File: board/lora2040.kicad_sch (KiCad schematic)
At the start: 22 parts, among them U1 RP2040, U2 MR20H40, U3 RFM9xBreakout, Y1 ABM8-272-T3

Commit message: added in sx1262 ref design
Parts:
- removed U3: RFM9xBreakout, RF_Module:HOPERF_RFM9XW_SMD, symbol symbols:RFM9xBreakout
- added C1: 47nF, custom-footprints:sx126x_C_0201, symbol Device:C_Small
- added C14, C15: 1nF, custom-footprints:sx126x_C_0201, symbol Device:C_Small
- added C16: 0.1uF, Capacitor_SMD:C_0402_1005Metric, symbol Device:C_Small
- added C17: 470nF, Capacitor_SMD:C_0402_1005Metric, symbol Device:C_Small
- added C18: 0.1uF, custom-footprints:sx126x_C_0201, symbol Device:C_Small
- added C2: 47pF, custom-footprints:sx126x_C_0201, symbol Device:C_Small
- added C21: 0.1uF, custom-footprints:sx126x_C_0201, symbol Device:C
- added C8: 39pF, custom-footprints:sx126x_C_0201, symbol Device:C_Small
- added J1: u.FL, Connector_Coaxial:U.FL_Hirose_U.FL-R-SMT-1_Vertical, symbol Connector:Conn_Coaxial
- added L1: 47nF, custom-footprints:sx126x_L_0402, symbol Device:L
- added L7: 15uH, custom-footprints:sx126x_L_0805, symbol Device:L
- added R3, R4: 100, custom-footprints:sx126x_R_0201, symbol Device:R_US
- added R9: 10K, custom-footprints:sx126x_R_0201, symbol Device:R_US
- added U1: SX1262IMLTRT, custom-footprints:VQFN24_4X4MM_SX126x, symbol RF:SX1262IMLTRT
- added U2: BGS12WN6E6327, Package_LGA:Infineon_PG-TSNP-6-10_0.7x1.1mm_0.7x1.1mm_P0.4mm, symbol RF_Switch:BGS12WN6E6327
- added U3: 0900FM15K0039, custom-footprints:0900FM15K0039, symbol Filter:0900FM15K0039
- added Y1: EXS00A-CS06465, custom-footprints:sx126x_Xtal, symbol Device:Crystal_GND24
- C10: renamed from C7; footprint Capacitor_SMD:C_0402_1005Metric -> custom-footprints:sx126x_C_0201
- C11: renamed from C8; footprint Capacitor_SMD:C_0402_1005Metric -> custom-footprints:sx126x_C_0201
- C12: renamed from C9; footprint Capacitor_SMD:C_0402_1005Metric -> custom-footprints:sx126x_C_0201
- C13: renamed from C10; footprint Capacitor_SMD:C_0402_1005Metric -> custom-footprints:sx126x_C_0201
- C3: renamed from C1; footprint Capacitor_SMD:C_0402_1005Metric -> custom-footprints:sx126x_C_0201
- C4: renamed from C2; footprint Capacitor_SMD:C_0402_1005Metric -> custom-footprints:sx126x_C_0201
- C5: footprint Capacitor_SMD:C_0402_1005Metric -> custom-footprints:sx126x_C_0201
- C6: renamed from C4; footprint Capacitor_SMD:C_0402_1005Metric -> custom-footprints:sx126x_C_0201
- R1: renamed from R4; footprint Resistor_SMD:R_0402_1005Metric -> custom-footprints:sx126x_R_0201
- R2: renamed from R5; footprint Resistor_SMD:R_0402_1005Metric -> custom-footprints:sx126x_R_0201
- R5: renamed from R6; footprint Resistor_SMD:R_0402_1005Metric -> custom-footprints:sx126x_R_0201
- R6: renamed from R1; footprint Resistor_SMD:R_0402_1005Metric -> custom-footprints:sx126x_R_0201
- R7: renamed from R3; footprint Resistor_SMD:R_0402_1005Metric -> custom-footprints:sx126x_R_0201
- R8: renamed from R2; footprint Resistor_SMD:R_0402_1005Metric -> custom-footprints:sx126x_R_0201
- U4: renamed from U2; value MR20H40 -> MR20H40 or AS3004204
- renumbered C11 to C19, C12 to C20, C3 to C7, C6 to C9, U1 to U5, Y1 to Y2
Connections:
- net +3V3: now also C21.2, R9.2
- net GND: now also C10.1, C11.1, C12.1, C13.1, C19.1, C20.1, Y2.2, Y2.4, C1.1, C14.1, C15.1, C16.2, C17.1, C18.2, C2.1, C21.1, J1.2 (Ext), U1.2 (GND), U1.20 (GND), U1.25 (GND), U1.5 (GND), U1.8 (GND), U2.2 (GND), U3.10 (GND), U3.2 (GND), U3.5 (GND), U3.7 (GND), U3.9 (GND), Y1.2, Y1.4; no longer Y2.1, Y2.3
- net XIN: now also Y2.1; no longer Y2.2
- net at U5.26 (RUN): now also R9.1
- net SPI0_MISO_RX: now reaches U5.27 (GPIO16)
- net SPI0_MISO_RX: now also U1.16 (MISO)
- net SPI0_CS: now reaches U5.28 (GPIO17)
- net SPI0_CS: now also U1.19 (NSS)
- net SPI0_SCK: now reaches U5.29 (GPIO18)
- net SPI0_SCK: now also U1.18 (SCK)
- net SPI0_MOSI_TX: now reaches U5.30 (GPIO19)
- net SPI0_MOSI_TX: now also U1.17 (MOSI)
- net RF_RST: now reaches U5.31 (GPIO20)
- net RF_RST: now also U1.15 (~{RESET})
- net RF_BUSY: now reaches U5.32 (GPIO21)
- net RF_BUSY: now also U1.14 (BUSY)
- net RF_DIO1: now reaches U5.37 (GPIO25)
- net RF_DIO1: now also U1.13 (DIO1)
- net at C4.2, R8.1: now also Y2.3; no longer Y2.4
- new net: L1.2, U1.23 (RFO), U3.1 (RFO)
- new net: U1.22 (RFI_N), U3.3 (RFI_N)
- new net: U1.21 (RFI_P), U3.4 (RFI_P)
- new net: U2.3 (RF1), U3.6 (SW_RFI)
- new net: U2.1 (RF2), U3.8 (SW_RFO)
- new net: C1.2, C2.2, L1.1, U1.24 (VR_PA)
- new net: C15.2, R3.1, U2.4 (VDD)
- new net: C17.2, L7.2, U1.7 (VREG)
- new net: C8.1, J1.1 (In)
- new net: L7.1, U1.9 (DCC_SW)
- new net: U1.3 (XTA), Y1.3
- new net: U1.4 (XTB), Y1.1
- new net: C8.2, U2.5 (RFIN)
- new net: C14.2, R4.2, U2.6 (CTRL)
- new net ANT_SW: R3.2
- new net RF_DIO2: R4.1, U1.12 (DIO2)
- new net RF_DIO3: U1.6 (DIO3)
- new net VDD_RF: C16.1, C18.1, U1.1 (VDD_IN), U1.10 (VBAT), U1.11 (VBAT_IO)
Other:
- note added: "Based on Semtech PCB_E588V01A v1a"
- note added: "short for bootloader"
- note removed: "Switch to SX126x?"
- moved on the sheet: C10, C11, C12, C13, C19, C20, C3, C4, C5, C6, C7, C9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

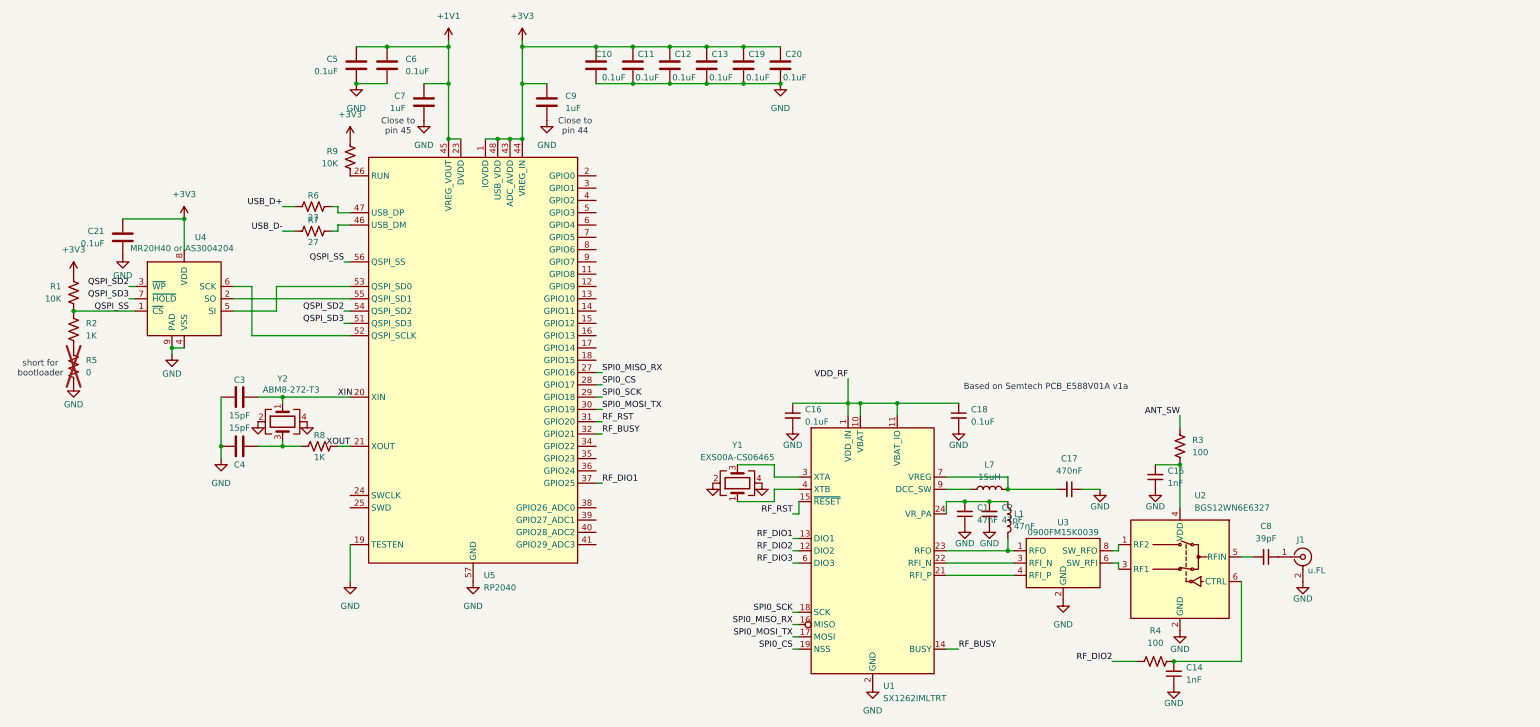
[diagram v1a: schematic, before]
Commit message: about to switch to TXCO
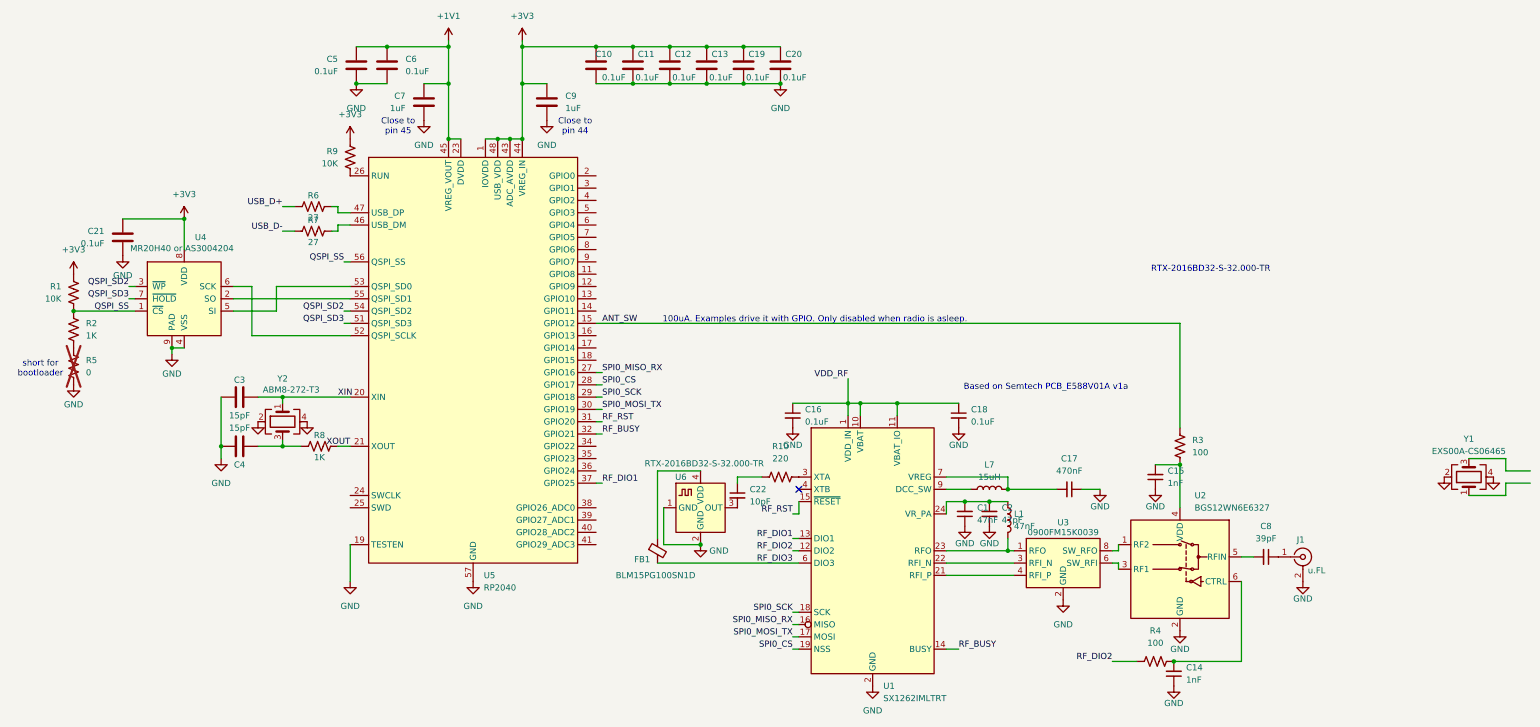
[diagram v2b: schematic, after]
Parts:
- added C22: 10pF, Capacitor_SMD:C_0402_1005Metric, symbol Device:C_Small
- added FB1: BLM15PG100SN1D, symbol Device:FerriteBead_Small
- added R10: 220, custom-footprints:sx126x_R_0201, symbol Device:R_US
- added U6: RTX-2016BD32-S-32.000-TR, custom-footprints:TXCO_2.0x1.6, symbol symbols:RTX-2016BD32-S-32.000-TR
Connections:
- net ANT_SW: now also U5.15 (GPIO12)
- net GND: now also U6.1 (GND), U6.2 (GND)
- net RF_DIO3: now also FB1.2
- net at U1.3 (XTA): now also R10.2; no longer Y1.3
- net at U1.4 (XTB): no longer Y1.1
- new net: FB1.1, U6.4 (VDD)
- new net: C22.2, U6.3 (OUT)
- new net: C22.1, R10.1
- no-connect marks 0 -> 1
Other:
- note added: "100uA. Examples drive it with GPIO. Only disabled when radio is asleep."
- note added: "RTX-2016BD32-S-32.000-TR"
- moved on the sheet: Y1

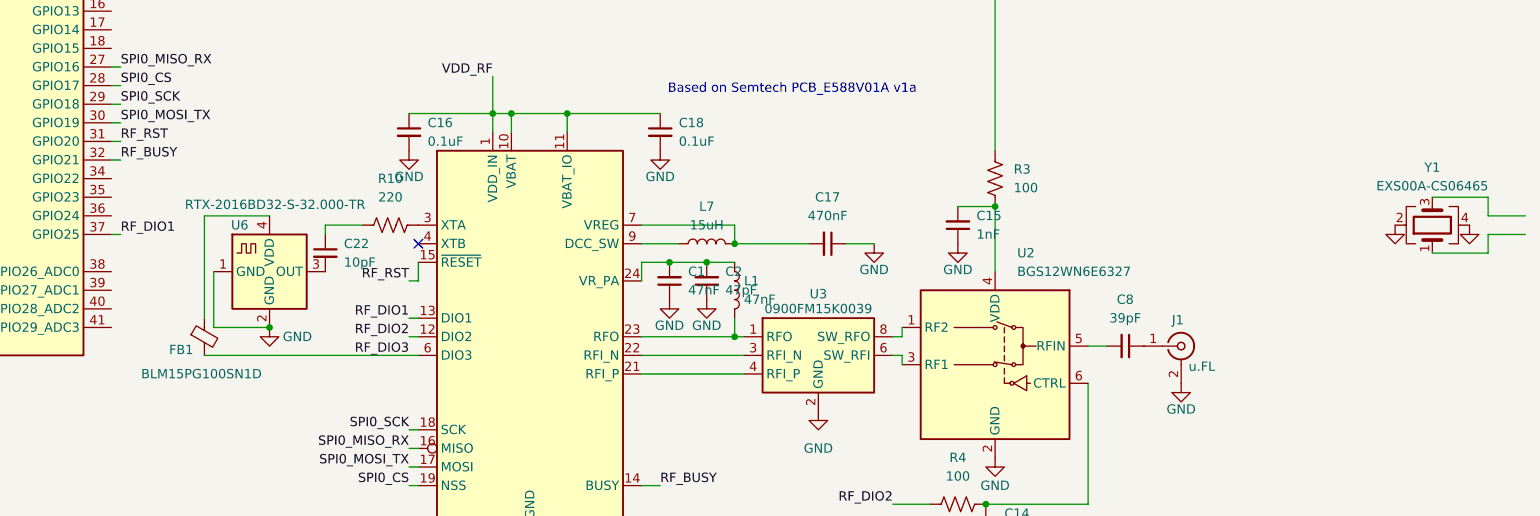
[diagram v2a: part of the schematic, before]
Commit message: changed to TXCO
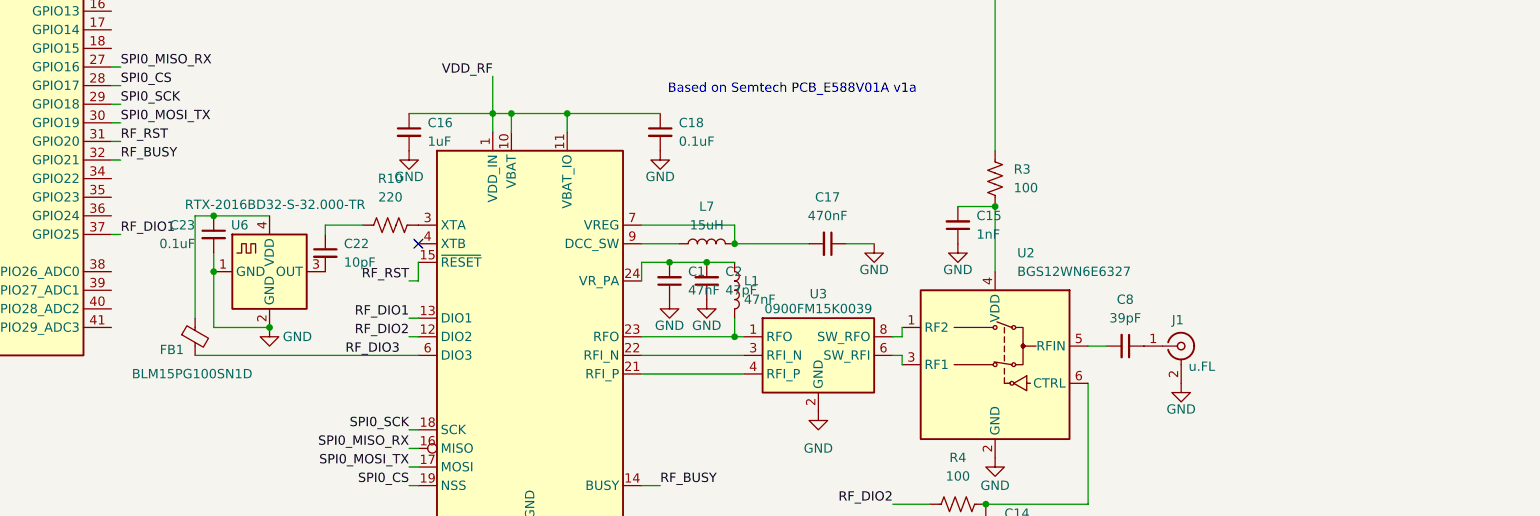
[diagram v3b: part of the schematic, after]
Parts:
- removed Y1: EXS00A-CS06465, custom-footprints:sx126x_Xtal, symbol Device:Crystal_GND24
- added C23: 0.1uF, custom-footprints:sx126x_C_0201, symbol Device:C_Small
- C16: value 0.1uF -> 1uF; footprint Capacitor_SMD:C_0402_1005Metric -> custom-footprints:sx126x_C_0402
- C17: footprint Capacitor_SMD:C_0402_1005Metric -> custom-footprints:sx126x_C_0402
- C22: footprint Capacitor_SMD:C_0402_1005Metric -> custom-footprints:sx126x_C_0201
- FB1: footprint (none) -> custom-footprints:sx126x_L_0402
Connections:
- net GND: now also C23.2
- net at FB1.1, U6.4 (VDD): now also C23.1
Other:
- moved on the sheet: FB1
